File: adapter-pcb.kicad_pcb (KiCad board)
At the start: 2 copper layers, 90.2 x 95.9 mm, 22 parts, among them J1 SS5-80-3.50-L-D-K-TR, J2 DM3BT-DSF-PEJS, U2 LTC4300A-1IMS8_PBF

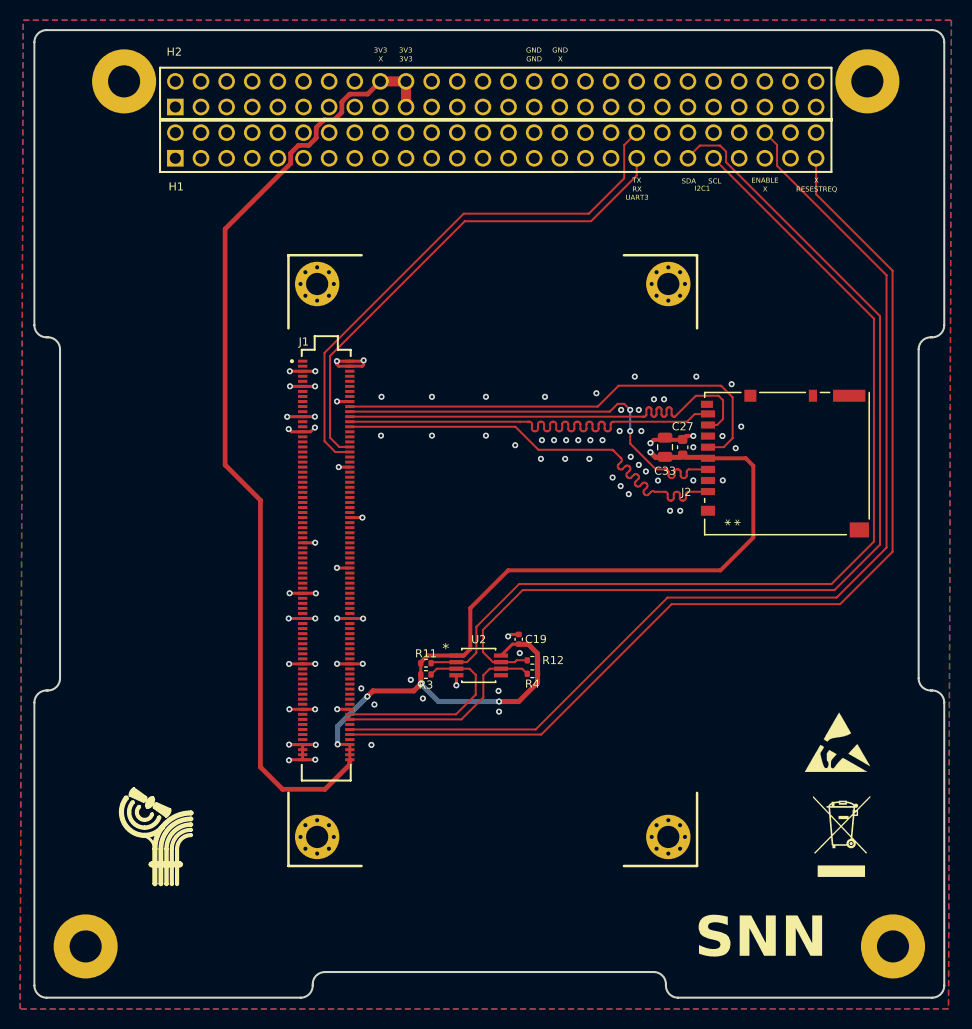
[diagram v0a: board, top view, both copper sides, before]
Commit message: Added level shifter and breakout for ethernet
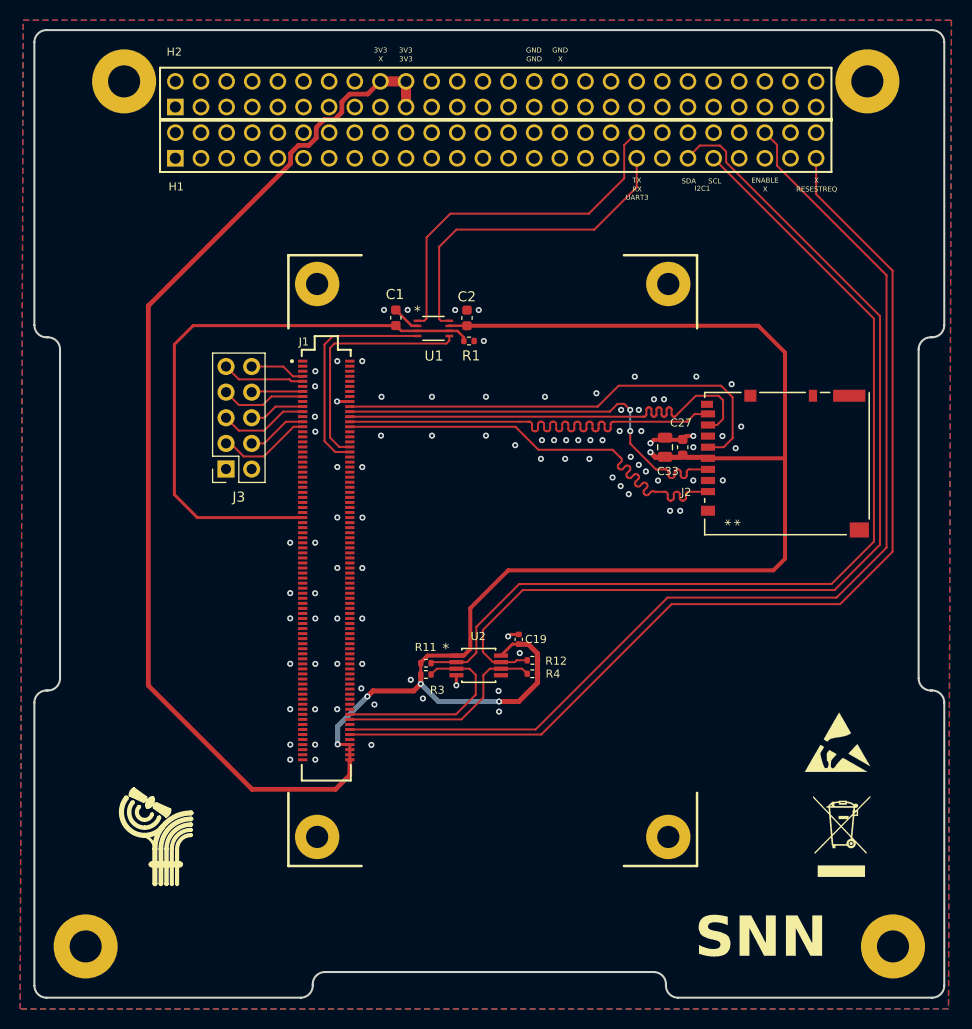
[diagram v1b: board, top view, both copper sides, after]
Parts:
- added C1: 100n, Capacitor_SMD:C_0603_1608Metric, F.Cu at (141.2, 75.0)
- added C2: 100n, Capacitor_SMD:C_0603_1608Metric, F.Cu at (148.3, 75.0)
- added J3: Conn_02x05_Odd_Even, Connector_PinSocket_2.54mm:PinSocket_2x05_P2.54mm_Vertical, F.Cu at (124.4, 90.0)
- added R1: 10K, Resistor_SMD:R_0402_1005Metric, F.Cu at (148.5, 77.3)
- added U1: TXS0102QDCURQ1, adapter:TXS0102QDCURQ1, F.Cu at (145.0, 76.1)
- MH5, MH6, MH7, MH8: footprint MountingHole:MountingHole_2.2mm_M2_Pad_Via -> MountingHole:MountingHole_2.2mm_M2_Pad
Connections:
- J1 pad 07: unconnected-(J1A-PHY_MDI0_P-Pad07) -> PHY_MDI0_P
- J1 pad 09: unconnected-(J1A-PHY_MDI0_N-Pad09) -> PHY_MDI0_N
- J1 pad 13: unconnected-(J1A-PHY_MDI1_P-Pad13) -> PHY_MDI1_P
- J1 pad 15: unconnected-(J1A-PHY_MDI1_N-Pad15) -> PHY_MDI1_N
- J1 pad 19: unconnected-(J1A-PHY_MDI2_P-Pad19) -> PHY_MDI2_P
- J1 pad 21: unconnected-(J1A-PHY_MDI2_N-Pad21) -> PHY_MDI2_N
- J1 pad 25: unconnected-(J1A-PHY_MDI3_P-Pad25) -> PHY_MDI3_P
- J1 pad 27: unconnected-(J1A-PHY_MDI3_N-Pad27) -> PHY_MDI3_N
- J1 pad 36: UART_RX -> UART-RXD
- J1 pad 38: UART_TX -> UART-TXD
- J1 pad 63: unconnected-(J1A-1V8_OUT-Pad63) -> +1V8
- MH5 pad 1: (no net) -> GND
- MH6 pad 1: (no net) -> GND
- MH7 pad 1: (no net) -> GND
- MH8 pad 1: (no net) -> GND
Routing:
- net +3V3: track 188.8 -> 250.4 mm
- net +1V8: track 0.00 -> 58.8 mm
- net GND: track 53.3 -> 10.8 mm, vias 86 -> 91
- net UART-RXD: track 0.00 -> 23.8 mm
- net UART-TXD: track 0.00 -> 22.1 mm
- net UART_TX: track 54.0 -> 36.5 mm
- net UART_RX: track 49.9 -> 33.1 mm
- net PHY_MDI3_N: track 0.00 -> 9.35 mm
- net PHY_MDI2_N: track 0.00 -> 8.90 mm
- net PHY_MDI1_N: track 0.00 -> 8.47 mm
- net PHY_MDI0_N: track 0.00 -> 8.21 mm
- net PHY_MDI3_P: track 0.00 -> 5.95 mm
- net PHY_MDI2_P: track 0.00 -> 5.52 mm
- net PHY_MDI0_P: track 0.00 -> 5.49 mm
- net PHY_MDI1_P: track 0.00 -> 5.09 mm
